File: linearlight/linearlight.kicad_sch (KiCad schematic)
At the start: 81 parts, among them J1 Screw_Terminal, J2 Conn_01x04_Pin, J3 Conn_01x19_Socket, J4 Conn_01x19_Socket, J5 Conn_01x04_Pin, Q1 FQP30N06, Q2 FQP30N06, Q3 FQP30N06, Q4 FQP30N06, Q5 2N3904, Q6 2N3904, Q7 2N3904, Q8 2N3904, U1 TLV5620CN, U2 ESP32 DevKitC, U3 MC33204, U4 LM4040LP-2.5, U5 TLV5620CN, U6 L7805

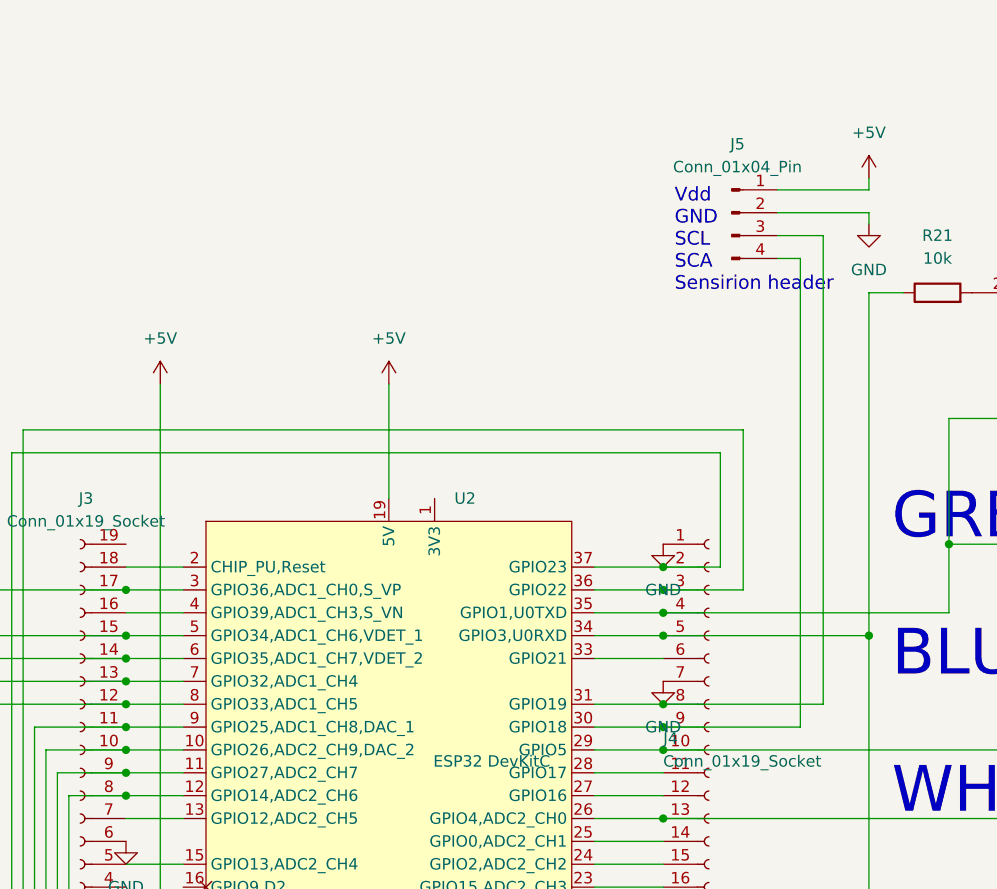
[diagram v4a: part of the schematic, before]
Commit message: Add cnx for spectrometer.
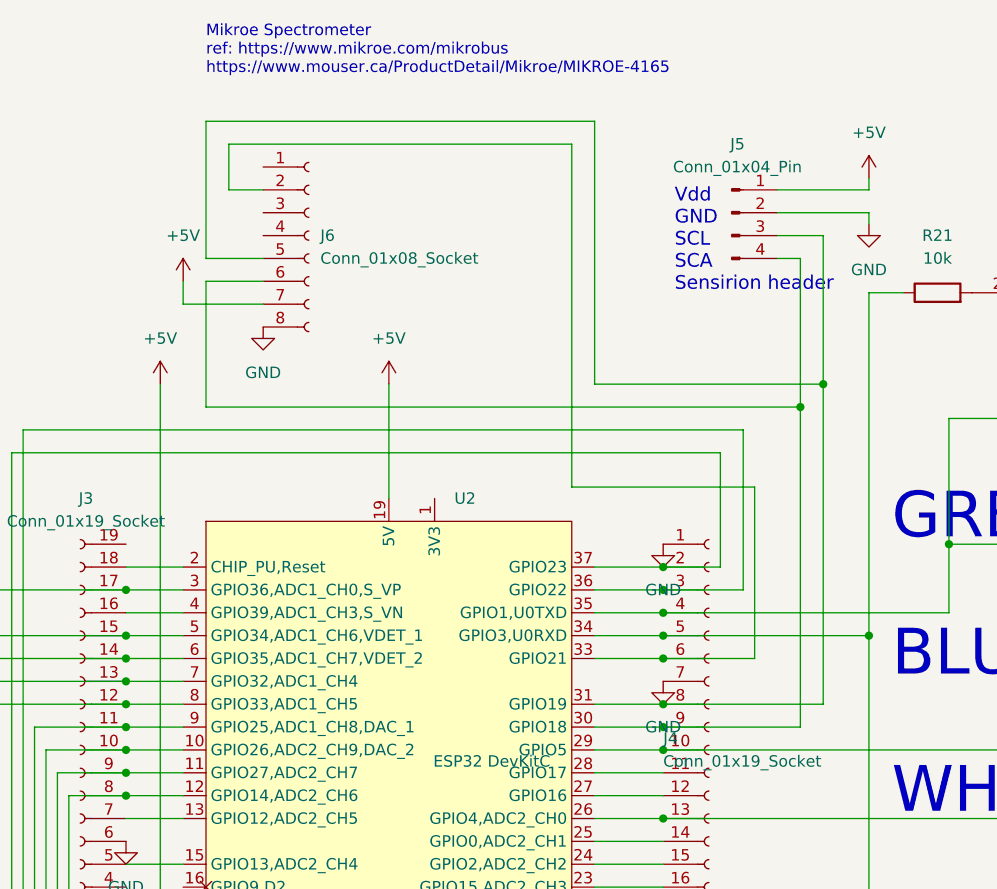
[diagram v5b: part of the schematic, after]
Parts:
- added J6: Conn_01x08_Socket, Connector_PinSocket_2.54mm:PinSocket_1x08_P2.54mm_Vertical, symbol Connector:Conn_01x08_Socket
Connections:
- net +5V: now also J6.7 (Pin_7)
- net GND: now also J6.8 (Pin_8)
- net at J4.8 (Pin_8), J5.3 (Pin_3), U2.31 (GPIO19): now also J6.5 (Pin_5)
- net at J4.9 (Pin_9), J5.4 (Pin_4), U2.30 (GPIO18): now also J6.6 (Pin_6)
- net at J4.6 (Pin_6), U2.33 (GPIO21): now also J6.2 (Pin_2)
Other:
- note added: "Mikroe Spectrometer ref: https://www.mikroe.com/mikrobus https://www.mouser.ca/ProductDetail/Mikroe/MIKROE-4165"
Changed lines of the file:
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@@
   (junction (at 299.72 143.51) (diameter 0) (color 0 0 0 0)
   )
+  (junction (at 148.59 90.17) (diameter 0) (color 0 0 0 0)
+  )
   (junction (at 264.16 102.87) (diameter 0) (color 0 0 0 0)
   )
@@
   (junction (at 170.18 168.91) (diameter 0) (color 0 0 0 0)
   )
+  (junction (at 133.35 118.11) (diameter 0) (color 0 0 0 0)
+  )
   (junction (at 121.92 160.02) (diameter 0) (color 0 0 0 0)
   )
@@
   (junction (at 187.96 121.92) (diameter 0) (color 0 0 0 0)
   )
+  (junction (at 151.13 87.63) (diameter 0) (color 0 0 0 0)
+  )
   (junction (at 165.1 105.41) (diameter 0) (color 0 0 0 0)
   )
@@
     (stroke (width 0) (type default))
   )
+  (wire (pts (xy 85.09 66.04) (xy 85.09 60.96))
+    (stroke (width 0) (type default))
+  )
   (wire (pts (xy 316.23 104.14) (xy 332.74 104.14))
     (stroke (width 0) (type default))
@@
     (stroke (width 0) (type default))
   )
+  (wire (pts (xy 143.51 99.06) (xy 143.51 118.11))
+    (stroke (width 0) (type default))
+  )
   (wire (pts (xy 238.76 72.39) (xy 238.76 90.17))
     (stroke (width 0) (type default))
@@
     (stroke (width 0) (type default))
   )
+  (wire (pts (xy 123.19 60.96) (xy 123.19 99.06))
+    (stroke (width 0) (type default))
+  )
   (wire (pts (xy 339.09 128.27) (xy 347.98 128.27))
     (stroke (width 0) (type default))
@@
     (stroke (width 0) (type default))
   )
+  (wire (pts (xy 85.09 60.96) (xy 123.19 60.96))
+    (stroke (width 0) (type default))
+  )
   (wire (pts (xy 125.73 128.27) (xy 133.35 128.27))
     (stroke (width 0) (type default))
@@
     (stroke (width 0) (type default))
   )
-  (wire (pts (xy 151.13 71.12) (xy 151.13 123.19))
+  (wire (pts (xy 151.13 71.12) (xy 151.13 87.63))
     (stroke (width 0) (type default))
   )
@@
     (stroke (width 0) (type default))
   )
+  (wire (pts (xy 151.13 87.63) (xy 151.13 123.19))
+    (stroke (width 0) (type default))
+  )
   (wire (pts (xy 236.22 210.82) (xy 259.08 210.82))
     (stroke (width 0) (type default))
@@
     (stroke (width 0) (type default))
   )
+  (wire (pts (xy 123.19 99.06) (xy 143.51 99.06))
+    (stroke (width 0) (type default))
+  )
+  (wire (pts (xy 82.55 58.42) (xy 82.55 73.66))
+    (stroke (width 0) (type default))
+  )
   (wire (pts (xy 332.74 104.14) (xy 332.74 110.49))
     (stroke (width 0) (type default))
@@
     (stroke (width 0) (type default))
   )
+  (wire (pts (xy 80.01 76.2) (xy 80.01 78.74))
+    (stroke (width 0) (type default))
+  )
   (wire (pts (xy 73.66 123.19) (xy 80.01 123.19))
     (stroke (width 0) (type default))
@@
     (stroke (width 0) (type default))
   )
+  (wire (pts (xy 82.55 58.42) (xy 125.73 58.42))
+    (stroke (width 0) (type default))
+  )
   (wire (pts (xy 44.45 158.75) (xy 44.45 198.12))
     (stroke (width 0) (type default))
@@
     (stroke (width 0) (type default))
   )
-  (wire (pts (xy 148.59 73.66) (xy 148.59 125.73))
+  (wire (pts (xy 148.59 73.66) (xy 148.59 90.17))
     (stroke (width 0) (type default))
   )
@@
     (stroke (width 0) (type default))
   )
+  (wire (pts (xy 88.9 76.2) (xy 82.55 76.2))
+    (stroke (width 0) (type default))
+  )
   (wire (pts (xy 328.93 99.06) (xy 332.74 99.06))
     (stroke (width 0) (type default))
@@
     (stroke (width 0) (type default))
   )
+  (wire (pts (xy 88.9 73.66) (xy 82.55 73.66))
+    (stroke (width 0) (type default))
+  )
   (wire (pts (xy 31.75 129.54) (xy 31.75 132.08))
     (stroke (width 0) (type default))
@@
     (stroke (width 0) (type default))
   )
+  (wire (pts (xy 148.59 90.17) (xy 148.59 125.73))
+    (stroke (width 0) (type default))
+  )
   (wire (pts (xy 175.26 72.39) (xy 180.34 72.39))
     (stroke (width 0) (type default))
@@
     (stroke (width 0) (type default))
   )
+  (wire (pts (xy 82.55 90.17) (xy 148.59 90.17))
+    (stroke (width 0) (type default))
+  )
   (wire (pts (xy 44.45 158.75) (xy 44.45 110.49))
     (stroke (width 0) (type default))
@@
     (stroke (width 0) (type default))
   )
-  (wire (pts (xy 125.73 118.11) (xy 133.35 118.11))
+  (wire (pts (xy 133.35 118.11) (xy 143.51 118.11))
     (stroke (width 0) (type default))
   )
@@
     (stroke (width 0) (type default))
   )
+  (wire (pts (xy 82.55 76.2) (xy 82.55 90.17))
+    (stroke (width 0) (type default))
+  )
   (wire (pts (xy 154.94 162.56) (xy 154.94 181.61))
     (stroke (width 0) (type default))
@@
     (stroke (width 0) (type default))
   )
+  (wire (pts (xy 88.9 66.04) (xy 85.09 66.04))
+    (stroke (width 0) (type default))
+  )
   (wire (pts (xy 259.08 143.51) (xy 299.72 143.51))
     (stroke (width 0) (type default))
@@
     (stroke (width 0) (type default))
   )
+  (wire (pts (xy 80.01 78.74) (xy 88.9 78.74))
+    (stroke (width 0) (type default))
+  )
   (wire (pts (xy 146.05 66.04) (xy 156.21 66.04))
     (stroke (width 0) (type default))
@@
     (stroke (width 0) (type default))
   )
+  (wire (pts (xy 125.73 118.11) (xy 133.35 118.11))
+    (stroke (width 0) (type default))
+  )
   (wire (pts (xy 77.47 87.63) (xy 77.47 151.13))
     (stroke (width 0) (type default))
@@
     (stroke (width 0) (type default))
   )
+  (wire (pts (xy 125.73 58.42) (xy 125.73 87.63))
+    (stroke (width 0) (type default))
+  )
   (wire (pts (xy 125.73 130.81) (xy 133.35 130.81))
     (stroke (width 0) (type default))
@@
     (stroke (width 0) (type default))
   )
+  (wire (pts (xy 125.73 87.63) (xy 151.13 87.63))
+    (stroke (width 0) (type default))
+  )
   (wire (pts (xy 170.18 168.91) (xy 181.61 168.91))
     (stroke (width 0) (type default))
@@
     (effects (font (size 5.08 5.08)) (justify left bottom))
   )
+  (text "Mikroe Spectrometer\nref: https://www.mikroe.com/mikrobus\nhttps://www.mouser.ca/ProductDetail/Mikroe/MIKROE-4165"
+    (at 82.55 53.34 0)
+    (effects (font (size 1.27 1.27)) (justify left bottom))
+  )
   (text "Power traces: \n2oz 10mil has max of 2.4A\nshould probably use 30mil ?\nref: https://www.raypcb.com/2-oz-copper-pcb"
     (at 303.53 88.9 0)
@@
     )
   )
+  (symbol (lib_id "power:GND") (at 88.9 81.28 0) (unit 1)
+    (in_bom yes) (on_board yes) (dnp no) (fields_autoplaced)
+    (property "Reference" "#PWR048" (at 88.9 87.63 0)
+      (effects (font (size 1.27 1.27)) hide)
+    )
+    (property "Value" "GND" (at 88.9 86.36 0)
+      (effects (font (size 1.27 1.27)))
+    )
+    (property "Footprint" "" (at 88.9 81.28 0)
+      (effects (font (size 1.27 1.27)) hide)
+    )
+    (property "Datasheet" "" (at 88.9 81.28 0)
+      (effects (font (size 1.27 1.27)) hide)
+    )
+    (pin "1")
+    (instances
+      (project "linearlight"
+        (path "/9f31f3ef-fa50-46f5-aec7-55370bc57602"
+          (reference "#PWR048") (unit 1)
+        )
+      )
+    )
+  )
   (symbol (lib_id "power:GND") (at 332.74 110.49 0) (unit 1)
     (in_bom yes) (on_board yes) (dnp no) (fields_autoplaced)
@@
     )
   )
+  (symbol (lib_id "Connector:Conn_01x08_Socket") (at 93.98 71.12 0) (unit 1)
+    (in_bom yes) (on_board yes) (dnp no) (fields_autoplaced)
+    (property "Reference" "J6" (at 95.25 71.12 0)
+      (effects (font (size 1.27 1.27)) (justify left))
+    )
+    (property "Value" "Conn_01x08_Socket" (at 95.25 73.66 0)
+      (effects (font (size 1.27 1.27)) (justify left))
+    )
+    (property "Footprint" "Connector_PinSocket_2.54mm:PinSocket_1x08_P2.54mm_Vertical" (at 93.98 71.12 0)
+      (effects (font (size 1.27 1.27)) hide)
+    )
+    (property "Datasheet" "~" (at 93.98 71.12 0)
+      (effects (font (size 1.27 1.27)) hide)
+    )
+    (pin "3")
+    (pin "4")
+    (pin "1")
+    (pin "5")
+    (pin "6")
+    (pin "2")
+    (pin "8")
+    (pin "7")
+    (instances
+      (project "linearlight"
+        (path "/9f31f3ef-fa50-46f5-aec7-55370bc57602"
+          (reference "J6") (unit 1)
+        )
+      )
+    )
+  )
   (symbol (lib_id "Connector:Conn_01x04_Pin") (at 140.97 68.58 0) (unit 1)
     (in_bom yes) (on_board yes) (dnp no) (fields_autoplaced)
@@
         )
       )
+    )
+  )
+  (symbol (lib_id "power:+5V") (at 80.01 76.2 0) (unit 1)
+    (in_bom yes) (on_board yes) (dnp no) (fields_autoplaced)
+    (property "Reference" "#PWR021" (at 80.01 80.01 0)
+      (effects (font (size 1.27 1.27)) hide)
+    )
+    (property "Value" "+5V" (at 80.01 71.12 0)
+      (effects (font (size 1.27 1.27)))
+    )
+    (property "Footprint" "" (at 80.01 76.2 0)
+      (effects (font (size 1.27 1.27)) hide)
+    )
+    (property "Datasheet" "" (at 80.01 76.2 0)
+      (effects (font (size 1.27 1.27)) hide)
+    )
+    (pin "1")
+    (instances
+      (project "linearlight"
+        (path "/9f31f3ef-fa50-46f5-aec7-55370bc57602"
+          (reference "#PWR021") (unit 1)
+        )
+      )

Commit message: Release candidate 3
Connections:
- net at D4.2 (A), R22.1: now also J4.8 (Pin_8), U2.31 (GPIO19); no longer J4.13 (Pin_13), U2.26 (GPIO4,ADC2_CH0)
- net at D2.2 (A), R26.1: now also J4.12 (Pin_12), U2.27 (GPIO16); no longer J4.4 (Pin_4), U2.35 (GPIO1,U0TXD)
- net at J4.6 (Pin_6), U2.33 (GPIO21): now also J5.4 (Pin_4), J6.6 (Pin_6); no longer J6.2 (Pin_2)
- net at J5.3 (Pin_3), J6.5 (Pin_5): now also J4.13 (Pin_13), U2.26 (GPIO4,ADC2_CH0); no longer J4.8 (Pin_8), U2.31 (GPIO19)
- net at J4.9 (Pin_9), U2.30 (GPIO18): now also J6.2 (Pin_2); no longer J5.4 (Pin_4), J6.6 (Pin_6)
- net at D5.2 (A), R21.1: now also J4.11 (Pin_11), U2.28 (GPIO17); no longer J4.5 (Pin_5), U2.34 (GPIO3,U0RXD)
- new net: J4.4 (Pin_4), U2.35 (GPIO1,U0TXD)
- new net: J4.5 (Pin_5), U2.34 (GPIO3,U0RXD)
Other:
- note removed: "in final version this R should be reduced e.g. to 0.1Ω to keep power < 0.5W"
- note removed: "max 285mV per channel (~1.9A) for 5m strip"
- moved on the sheet: R30, R31, R32

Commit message: Add usage text
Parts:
- R3: value 3.3k -> 2.2k
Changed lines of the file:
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@@
       (effects (font (size 1.27 1.27)) (justify left))
     )
-    (property "Value" "3.3k" (at 34.29 127 0)
+    (property "Value" "2.2k" (at 34.29 127 0)
       (effects (font (size 1.27 1.27)) (justify left))
     )
